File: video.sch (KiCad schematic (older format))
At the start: 31 parts, among them CN10 COMPOSITE, CN9 VIDEO_DB23M, U4 DENISE, U40 74LS245, U41 74LS245

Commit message: Work in progress
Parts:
- E402, E403, E404, E405, E431, E432, E433, E434, E435: footprint (none) -> Raemixx500:EMI_Filter_Long
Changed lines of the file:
@@
 F 0 "E405" H 14655 3380 50  0000 C CNN
 F 1 "10n" H 14820 3140 50  0000 C CNN
-F 2 "" V 14655 3185 50  0001 C CNN
+F 2 "Raemixx500:EMI_Filter_Long" V 14655 3185 50  0001 C CNN
 F 3 "http://www.murata.com/~/media/webrenewal/support/library/catalog/products/emc/emifil/c31e.ashx?la=en-gb" V 14655 3185 50  0001 C CNN
 	1    14655 3185
@@
 F 0 "E403" H 14430 2650 50  0000 C CNN
 F 1 "10n" H 14580 2400 50  0000 C CNN
-F 2 "" V 14430 2445 50  0001 C CNN
+F 2 "Raemixx500:EMI_Filter_Long" V 14430 2445 50  0001 C CNN
 F 3 "http://www.murata.com/~/media/webrenewal/support/library/catalog/products/emc/emifil/c31e.ashx?la=en-gb" V 14430 2445 50  0001 C CNN
 	1    14430 2445
@@
 F 0 "E404" H 14540 3005 50  0000 C CNN
 F 1 "10n" H 14690 2760 50  0000 C CNN
-F 2 "" V 14540 2805 50  0001 C CNN
+F 2 "Raemixx500:EMI_Filter_Long" V 14540 2805 50  0001 C CNN
 F 3 "http://www.murata.com/~/media/webrenewal/support/library/catalog/products/emc/emifil/c31e.ashx?la=en-gb" V 14540 2805 50  0001 C CNN
 	1    14540 2805
@@
 F 0 "E433" V 14115 5125 50  0000 C CNN
 F 1 "Ferrite_Bead_Small" V 14009 4965 50  0001 C CNN
-F 2 "" V 14085 4965 50  0001 C CNN
+F 2 "Raemixx500:EMI_Filter_Long" V 14085 4965 50  0001 C CNN
 F 3 "~" H 14155 4965 50  0001 C CNN
 	1    14155 4965
@@
 F 0 "E432" V 14115 5325 50  0000 C CNN
 F 1 "Ferrite_Bead_Small" V 14009 5165 50  0001 C CNN
-F 2 "" V 14085 5165 50  0001 C CNN
+F 2 "Raemixx500:EMI_Filter_Long" V 14085 5165 50  0001 C CNN
 F 3 "~" H 14155 5165 50  0001 C CNN
 	1    14155 5165
@@
 F 0 "E431" V 14115 5525 50  0000 C CNN
 F 1 "Ferrite_Bead_Small" V 14009 5365 50  0001 C CNN
-F 2 "" V 14085 5365 50  0001 C CNN
+F 2 "Raemixx500:EMI_Filter_Long" V 14085 5365 50  0001 C CNN
 F 3 "~" H 14155 5365 50  0001 C CNN
 	1    14155 5365
@@
 F 0 "E402" H 13000 6135 50  0000 C CNN
 F 1 "150p" H 13165 5895 50  0000 C CNN
-F 2 "" V 13000 5940 50  0001 C CNN
+F 2 "Raemixx500:EMI_Filter_Long" V 13000 5940 50  0001 C CNN
 F 3 "http://www.murata.com/~/media/webrenewal/support/library/catalog/products/emc/emifil/c31e.ashx?la=en-gb" V 13000 5940 50  0001 C CNN
 	1    13000 5940
@@
 F 0 "E434" H 13460 2665 50  0000 C CNN
 F 1 "150p" H 13625 2425 50  0000 C CNN
-F 2 "" V 13460 2470 50  0001 C CNN
+F 2 "Raemixx500:EMI_Filter_Long" V 13460 2470 50  0001 C CNN
 F 3 "http://www.murata.com/~/media/webrenewal/support/library/catalog/products/emc/emifil/c31e.ashx?la=en-gb" V 13460 2470 50  0001 C CNN
 	1    13460 2470
@@
 F 0 "E435" V 8660 4135 50  0000 C CNN
 F 1 "Ferrite_Bead_Small" V 8554 3975 50  0001 C CNN
-F 2 "" V 8630 3975 50  0001 C CNN
+F 2 "Raemixx500:EMI_Filter_Long" V 8630 3975 50  0001 C CNN
 F 3 "~" H 8700 3975 50  0001 C CNN
 	1    8700 3975

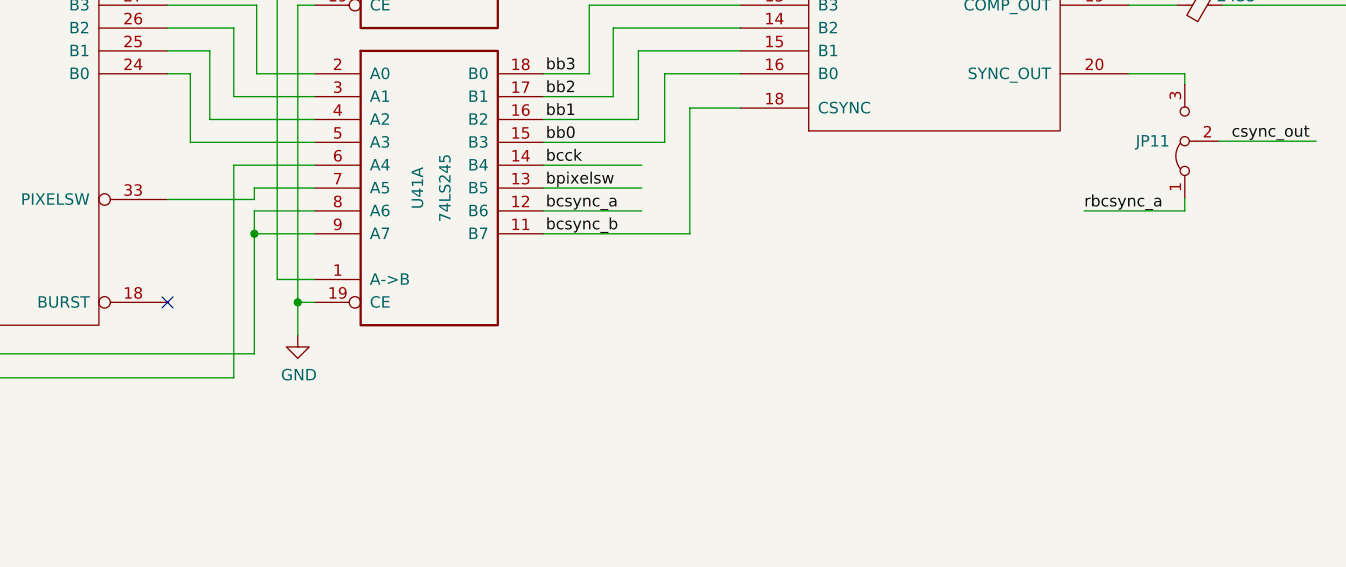
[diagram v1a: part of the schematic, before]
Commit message: Almost all components positioned
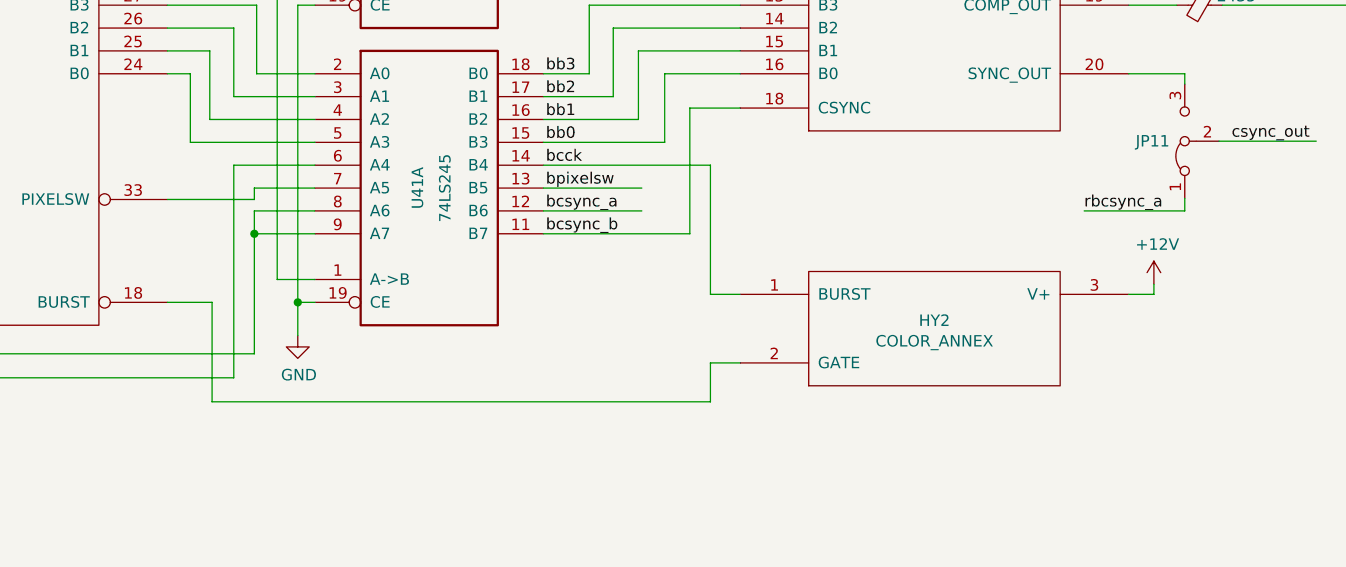
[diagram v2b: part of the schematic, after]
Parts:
- added HY2: COLOR_ANNEX, Connector_PinHeader_2.54mm:PinHeader_1x03_P2.54mm_Vertical, symbol VIDIOT:VIDIOT_ANNEX
- E406: footprint (none) -> Raemixx500:EMI_Filter_Short
- R409: footprint (none) -> Raemixx500:C_Axial_L9.0mm_D3.2mm_P12.70mm
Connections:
- wire segments 291 -> 300
- no-connect marks 3 -> 2
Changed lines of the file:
@@
 Wire Wire Line
 	2515 4775 2685 4775
-NoConn ~ 4185 5275
 Wire Wire Line
 	13940 6110 14200 6110
@@
 Text Label 12125 4465 0    50   ~ 0
 bb0
-Wire Wire Line
-	5830 4675 6260 4675
 Wire Wire Line
 	5830 4775 6260 4775
@@
 F 0 "E406" H 3450 7395 50  0000 C CNN
 F 1 "10n" H 3615 7155 50  0000 C CNN
-F 2 "" V 3450 7200 50  0001 C CNN
+F 2 "Raemixx500:EMI_Filter_Short" V 3450 7200 50  0001 C CNN
 F 3 "http://www.murata.com/~/media/webrenewal/support/library/catalog/products/emc/emifil/c31e.ashx?la=en-gb" V 3450 7200 50  0001 C CNN
 	1    3450 7200
@@
 F 0 "R409" H 9750 4385 50  0000 L CNN
 F 1 "150" V 9740 4165 50  0000 L CNN
-F 2 "" V 9670 4235 50  0001 C CNN
+F 2 "Raemixx500:C_Axial_L9.0mm_D3.2mm_P12.70mm" V 9670 4235 50  0001 C CNN
 F 3 "~" H 9740 4235 50  0001 C CNN
 	1    9740 4235
@@
 Wire Wire Line
 	8390 3975 8600 3975
+$Comp
+L VIDIOT:VIDIOT_ANNEX HY2
+U 1 1 5D5227DD
+P 7540 5390
+F 0 "HY2" H 7540 5425 50  0000 C CNN
+F 1 "COLOR_ANNEX" H 7540 5335 50  0000 C CNN
+F 2 "Connector_PinHeader_2.54mm:PinHeader_1x03_P2.54mm_Vertical" H 7540 5390 50  0001 C CNN
+F 3 "https://github.com/SukkoPera/OpenAmigaVideoHybrid" H 7540 5390 50  0001 C CNN
+	1    7540 5390
+	1    0    0    -1
+$EndComp
+Wire Wire Line
+	6560 4675 6560 5240
+Wire Wire Line
+	6560 5240 6690 5240
+Wire Wire Line
+	5830 4675 6560 4675
+Wire Wire Line
+	4185 5275 4380 5275
+Wire Wire Line
+	4380 5275 4380 5710
+Wire Wire Line
+	4380 5710 6560 5710
+Wire Wire Line
+	6560 5710 6560 5540
+Wire Wire Line
+	6560 5540 6690 5540
+$Comp
+L power:+12V #PWR0265
+U 1 1 5D59CEB5
+P 8500 5195
+F 0 "#PWR0265" H 8500 5045 50  0001 C CNN
+F 1 "+12V" H 8515 5368 50  0000 C CNN
+F 2 "" H 8500 5195 50  0001 C CNN
+F 3 "" H 8500 5195 50  0001 C CNN
+	1    8500 5195
+	1    0    0    -1
+$EndComp
+Wire Wire Line
+	8390 5240 8500 5240
+Wire Wire Line
+	8500 5240 8500 5195
 Wire Bus Line
 	2005 3775 2005 4475

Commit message: Work in progress
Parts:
- removed E431, E432, E433, E435: Ferrite_Bead_Small, Raemixx500:EMI_Filter_Long, symbol Device:Ferrite_Bead_Small
- added E431, E432, E433, E435: FERR, Raemixx500:EMI_Filter_Long, symbol emi_filter_lcl_small:EMI_Filter_LCL
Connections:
- wire segments 300 -> 314
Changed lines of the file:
@@
 Wire Wire Line
 	14380 5565 12745 5565
-Text GLabel 12395 5565 0    50   Output ~ 0
-~XCLKEN
 Wire Wire Line
 	6030 3975 6690 3975
@@
 Wire Wire Line
 	13940 4265 13940 4465
-$Comp
-L Device:Ferrite_Bead_Small E433
-U 1 1 5CFAFD37
-P 14155 4965
-F 0 "E433" V 14115 5125 50  0000 C CNN
-F 1 "Ferrite_Bead_Small" V 14009 4965 50  0001 C CNN
-F 2 "Raemixx500:EMI_Filter_Long" V 14085 4965 50  0001 C CNN
-F 3 "~" H 14155 4965 50  0001 C CNN
-	1    14155 4965
-	0    1    1    0
-$EndComp
-$Comp
-L Device:Ferrite_Bead_Small E432
-U 1 1 5CFAFFD0
-P 14155 5165
-F 0 "E432" V 14115 5325 50  0000 C CNN
-F 1 "Ferrite_Bead_Small" V 14009 5165 50  0001 C CNN
-F 2 "Raemixx500:EMI_Filter_Long" V 14085 5165 50  0001 C CNN
-F 3 "~" H 14155 5165 50  0001 C CNN
-	1    14155 5165
-	0    1    1    0
-$EndComp
-$Comp
-L Device:Ferrite_Bead_Small E431
-U 1 1 5CFB0114
-P 14155 5365
-F 0 "E431" V 14115 5525 50  0000 C CNN
-F 1 "Ferrite_Bead_Small" V 14009 5365 50  0001 C CNN
-F 2 "Raemixx500:EMI_Filter_Long" V 14085 5365 50  0001 C CNN
-F 3 "~" H 14155 5365 50  0001 C CNN
-	1    14155 5365
-	0    1    1    0
-$EndComp
-Wire Wire Line
-	14255 4965 14380 4965
-Wire Wire Line
-	14255 5165 14380 5165
-Wire Wire Line
-	14255 5365 14380 5365
-Wire Wire Line
-	14055 4965 12105 4965
-Wire Wire Line
-	14055 5165 12105 5165
-Wire Wire Line
-	14055 5365 12105 5365
-Text Label 12105 4965 0    50   ~ 0
+Text Label 10880 4965 0    50   ~ 0
 ab
-Text Label 12105 5165 0    50   ~ 0
+Text Label 10880 5165 0    50   ~ 0
 ag
-Text Label 12105 5365 0    50   ~ 0
+Text Label 10880 5365 0    50   ~ 0
 ar
 Wire Wire Line
@@
 	13385 5265 13385 5840
 Wire Wire Line
-	12990 3765 12010 3765
-Wire Wire Line
-	12010 3765 12010 5840
-Wire Wire Line
-	12010 5840 12700 5840
-Text Label 12460 5840 0    50   ~ 0
+	12990 3765 12540 3765
+Wire Wire Line
+	12540 3765 12540 5840
+Wire Wire Line
+	12540 5840 12700 5840
+Text Label 12540 5840 1    50   ~ 0
 cck_c
 $Comp
@@
 Connection ~ 12745 5565
 Wire Wire Line
-	12745 5565 12395 5565
+	12745 5565 11210 5565
 Wire Wire Line
 	12550 2970 12550 2835
@@
 rbcsync_a
 $Comp
-L Device:Ferrite_Bead_Small E435
-U 1 1 5D99AF23
-P 8700 3975
-F 0 "E435" V 8660 4135 50  0000 C CNN
-F 1 "Ferrite_Bead_Small" V 8554 3975 50  0001 C CNN
-F 2 "Raemixx500:EMI_Filter_Long" V 8630 3975 50  0001 C CNN
-F 3 "~" H 8700 3975 50  0001 C CNN
-	1    8700 3975
-	0    1    1    0
-$EndComp
-$Comp
 L Connector:Conn_Coaxial CN?
 U 1 1 5D9B0BDD
@@
 	1    0    0    -1
 $EndComp
-Wire Wire Line
-	8800 3975 9740 3975
 $Comp
 L power:GND #PWR0264
@@
 Wire Wire Line
 	9740 4385 9740 4460
-Wire Wire Line
-	9740 4460 10180 4460
 Connection ~ 10180 4460
 Wire Wire Line
@@
 Wire Wire Line
 	13460 2965 13940 2965
-Wire Wire Line
-	8390 3975 8600 3975
 $Comp
 L VIDIOT:VIDIOT_ANNEX HY2
@@
 Wire Wire Line
 	8500 5240 8500 5195
+$Comp
+L emi_filter_lcl_small:EMI_Filter_LCL E?
+U 1 1 5DD342FD
+P 12100 5065
+AR Path="/5E7E9EC4/5DD342FD" Ref="E?"  Part="1"
+AR Path="/5CBA5669/5DD342FD" Ref="E433"  Part="1"
+F 0 "E433" H 11960 5255 50  0000 C CNN
+F 1 "FERR" H 11910 5040 50  0000 C CNN
+F 2 "Raemixx500:EMI_Filter_Long" V 12100 5065 50  0001 C CNN
+F 3 "http://www.murata.com/~/media/webrenewal/support/library/catalog/products/emc/emifil/c31e.ashx?la=en-gb" V 12100 5065 50  0001 C CNN
+	1    12100 5065
+	1    0    0    -1
+$EndComp
+$Comp
+L emi_filter_lcl_small:EMI_Filter_LCL E?
+U 1 1 5DD4BEEC
+P 12100 5465
+AR Path="/5E7E9EC4/5DD4BEEC" Ref="E?"  Part="1"
+AR Path="/5CBA5669/5DD4BEEC" Ref="E431"  Part="1"
+F 0 "E431" H 11960 5655 50  0000 C CNN
+F 1 "FERR" H 11910 5440 50  0000 C CNN
+F 2 "Raemixx500:EMI_Filter_Long" V 12100 5465 50  0001 C CNN
+F 3 "http://www.murata.com/~/media/webrenewal/support/library/catalog/products/emc/emifil/c31e.ashx?la=en-gb" V 12100 5465 50  0001 C CNN
+	1    12100 5465
+	1    0    0    -1
+$EndComp
+$Comp
+L emi_filter_lcl_small:EMI_Filter_LCL E?
+U 1 1 5DD7EF86
+P 11450 5265
+AR Path="/5E7E9EC4/5DD7EF86" Ref="E?"  Part="1"
+AR Path="/5CBA5669/5DD7EF86" Ref="E432"  Part="1"
+F 0 "E432" H 11310 5455 50  0000 C CNN
+F 1 "FERR" H 11260 5240 50  0000 C CNN
+F 2 "Raemixx500:EMI_Filter_Long" V 11450 5265 50  0001 C CNN
+F 3 "http://www.murata.com/~/media/webrenewal/support/library/catalog/products/emc/emifil/c31e.ashx?la=en-gb" V 11450 5265 50  0001 C CNN
+	1    11450 5265
+	1    0    0    -1
+$EndComp
+Wire Wire Line
+	11800 4965 10880 4965
+Wire Wire Line
+	11150 5165 10880 5165
+Wire Wire Line
+	11800 5365 10880 5365
+Wire Wire Line
+	12400 4965 14380 4965
+Wire Wire Line
+	11750 5165 14380 5165
+Wire Wire Line
+	12400 5365 14380 5365
+Text GLabel 11210 5565 0    50   Output ~ 0
+~XCLKEN
+Connection ~ 14380 4965
+Wire Wire Line
+	14380 4965 14865 4965
+Connection ~ 14380 5165
+Wire Wire Line
+	14380 5165 14865 5165
+Connection ~ 14380 5365
+Wire Wire Line
+	14380 5365 14865 5365
+Wire Wire Line
+	12100 5115 12100 5225
+Wire Wire Line
+	12100 5225 11730 5225
+Wire Wire Line
+	11730 5225 11730 5420
+Wire Wire Line
+	11450 5315 11450 5420
+Wire Wire Line
+	11450 5420 11730 5420
+Connection ~ 11730 5420
+Wire Wire Line
+	11730 5420 11730 5625
+Wire Wire Line
+	12100 5515 12100 5625
+Wire Wire Line
+	12100 5625 11730 5625
+Connection ~ 11730 5625
+Wire Wire Line
+	11730 5625 11730 5775
+$Comp
+L power:GND #PWR0269
+U 1 1 5DF44B74
+P 11730 5775
+F 0 "#PWR0269" H 11730 5525 50  0001 C CNN
+F 1 "GND" H 11735 5602 50  0000 C CNN
+F 2 "" H 11730 5775 50  0001 C CNN
+F 3 "" H 11730 5775 50  0001 C CNN
+	1    11730 5775
+	1    0    0    -1
+$EndComp
+Wire Wire Line
+	8390 3975 8820 3975
+Wire Wire Line
+	9420 3975 9740 3975
+$Comp
+L emi_filter_lcl_small:EMI_Filter_LCL E?
+U 1 1 5DF6B27A
+P 9120 4075
+AR Path="/5E7E9EC4/5DF6B27A" Ref="E?"  Part="1"
+AR Path="/5CBA5669/5DF6B27A" Ref="E435"  Part="1"
+F 0 "E435" H 8980 4265 50  0000 C CNN
+F 1 "FERR" H 8930 4050 50  0000 C CNN
+F 2 "Raemixx500:EMI_Filter_Long" V 9120 4075 50  0001 C CNN
+F 3 "http://www.murata.com/~/media/webrenewal/support/library/catalog/products/emc/emifil/c31e.ashx?la=en-gb" V 9120 4075 50  0001 C CNN
+	1    9120 4075
+	1    0    0    -1
+$EndComp
+Wire Wire Line
+	9120 4125 9120 4460
+Wire Wire Line
+	9120 4460 9740 4460
 Wire Bus Line
 	2005 3775 2005 4475
 Wire Bus Line
 	2005 2075 2005 3575
+Connection ~ 9740 4460
+Wire Wire Line
+	9740 4460 10180 4460
 $EndSCHEMATC

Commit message: Top layer done!
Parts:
- C403: footprint (none) -> Raemixx500:VariCap
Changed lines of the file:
@@
 F 0 "C403" H 2195 5561 50  0000 L CNN
 F 1 "47P" H 2195 5470 50  0000 L CNN
-F 2 "" H 2080 5515 50  0001 C CNN
+F 2 "Raemixx500:VariCap" H 2080 5515 50  0001 C CNN
 F 3 "~" H 2080 5515 50  0001 C CNN
 	1    2080 5515
@@
 Wire Wire Line
 	9120 4460 9740 4460
+Connection ~ 9740 4460
+Wire Wire Line
+	9740 4460 10180 4460
 Wire Bus Line
 	2005 3775 2005 4475
 Wire Bus Line
 	2005 2075 2005 3575
-Connection ~ 9740 4460
-Wire Wire Line
-	9740 4460 10180 4460
 $EndSCHEMATC

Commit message: Fix shielding of D-Sub connectors
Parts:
- CN9: footprint Raemixx500:DB_23 -> Raemixx500:DB_23M
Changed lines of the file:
@@
 F 0 "CN9" H 14859 4468 50  0000 L CNN
 F 1 "VIDEO_DB23M" H 14859 4377 50  0000 L CNN
-F 2 "Raemixx500:DB_23" H 14680 4565 50  0001 C CNN
+F 2 "Raemixx500:DB_23M" H 14680 4565 50  0001 C CNN
 F 3 " ~" H 14680 4565 50  0001 C CNN
 	1    14680 4565

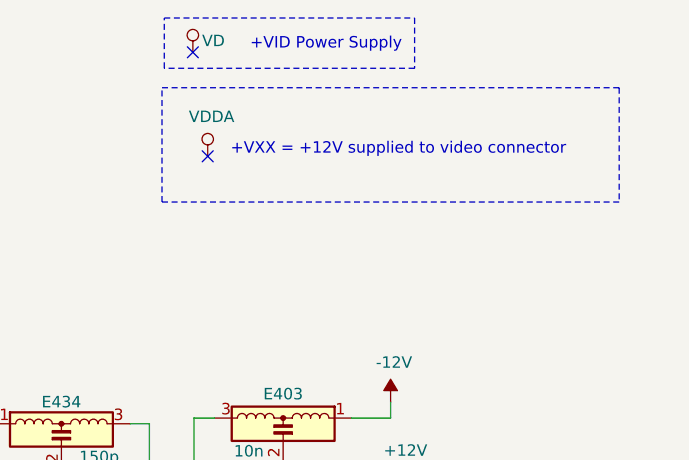
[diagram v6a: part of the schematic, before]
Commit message: Fix a lot of ERC/DRC errors
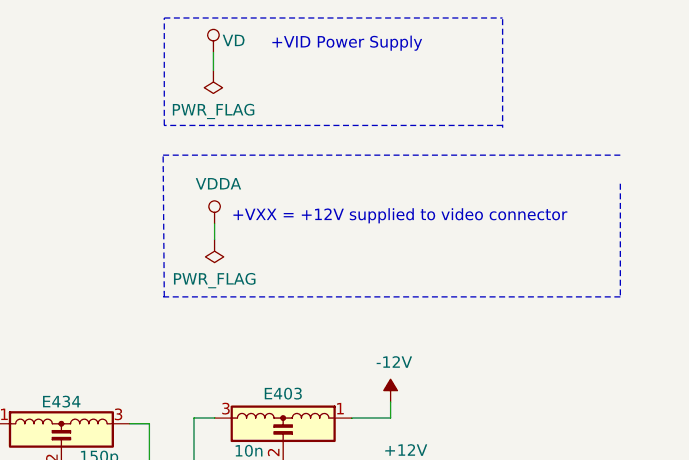
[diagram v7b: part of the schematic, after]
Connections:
- wire segments 314 -> 316
- no-connect marks 2 -> 0
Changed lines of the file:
@@
 EESchema Schematic File Version 4
-LIBS:Raemix500-cache
-EELAYER 29 0
+EELAYER 30 0
 EELAYER END
 $Descr A3 16535 11693
@@
 L power:VD #PWR0124
 U 1 1 5CBFE4AA
-P 14035 745
-F 0 "#PWR0124" H 14035 595 50  0001 C CNN
-F 1 "VD" H 14125 795 50  0000 C CNN
-F 2 "" H 14035 745 50  0001 C CNN
-F 3 "" H 14035 745 50  0001 C CNN
-	1    14035 745
-	1    0    0    -1
-$EndComp
-NoConn ~ 14035 745
-Text Notes 14950 740  2    50   ~ 0
+P 14125 745
+F 0 "#PWR0124" H 14125 595 50  0001 C CNN
+F 1 "VD" H 14215 795 50  0000 C CNN
+F 2 "" H 14125 745 50  0001 C CNN
+F 3 "" H 14125 745 50  0001 C CNN
+	1    14125 745
+	1    0    0    -1
+$EndComp
+Text Notes 15040 740  2    50   ~ 0
 +VID Power Supply
 Wire Notes Line
-	13910 595  15005 595
+	13910 595  15390 595
 Wire Notes Line
-	15005 595  15005 815
+	15390 600  15390 1075
 Wire Notes Line
-	15005 815  13910 815
+	15390 1065 13910 1065
 Wire Notes Line
-	13910 815  13910 595
+	13910 1065 13910 595
 $Comp
 L VIDIOT:VIDIOT HY1
@@
 L power:VDDA #PWR0206
 U 1 1 5D22310F
-P 14100 1200
-F 0 "#PWR0206" H 14100 1050 50  0001 C CNN
-F 1 "VDDA" H 14117 1373 50  0000 C CNN
-F 2 "" H 14100 1200 50  0001 C CNN
-F 3 "" H 14100 1200 50  0001 C CNN
-	1    14100 1200
-	1    0    0    -1
-$EndComp
-Text Notes 14200 1200 0    50   ~ 0
+P 14130 1495
+F 0 "#PWR0206" H 14130 1345 50  0001 C CNN
+F 1 "VDDA" H 14147 1668 50  0000 C CNN
+F 2 "" H 14130 1495 50  0001 C CNN
+F 3 "" H 14130 1495 50  0001 C CNN
+	1    14130 1495
+	1    0    0    -1
+$EndComp
+Text Notes 14205 1495 0    50   ~ 0
 +VXX = +12V supplied to video connector
-NoConn ~ 14100 1200
 Wire Notes Line
-	13900 900  15900 900
+	13905 1195 15905 1195
 Wire Notes Line
-	15900 900  15900 1400
+	15905 1320 15905 1820
 Wire Notes Line
-	15900 1400 13900 1400
+	15905 1815 13905 1815
 Wire Notes Line
-	13900 1400 13900 900
+	13910 1815 13905 1195
 $Comp
 L power:VDDA #PWR0207
@@
 Wire Wire Line
 	9740 4460 10180 4460
+$Comp
+L power:PWR_FLAG #FLG0101
+U 1 1 5EAB4BF3
+P 14130 1565
+F 0 "#FLG0101" H 14130 1640 50  0001 C CNN
+F 1 "PWR_FLAG" H 14130 1738 50  0000 C CNN
+F 2 "" H 14130 1565 50  0001 C CNN
+F 3 "~" H 14130 1565 50  0001 C CNN
+	1    14130 1565
+	-1   0    0    1
+$EndComp
+Wire Wire Line
+	14130 1565 14130 1495
+$Comp
+L power:PWR_FLAG #FLG0102
+U 1 1 5EAEA0A6
+P 14125 825
+F 0 "#FLG0102" H 14125 900 50  0001 C CNN
+F 1 "PWR_FLAG" H 14125 998 50  0000 C CNN
+F 2 "" H 14125 825 50  0001 C CNN
+F 3 "~" H 14125 825 50  0001 C CNN
+	1    14125 825
+	-1   0    0    1
+$EndComp
+Wire Wire Line
+	14125 825  14125 745
 Wire Bus Line
 	2005 3775 2005 4475
